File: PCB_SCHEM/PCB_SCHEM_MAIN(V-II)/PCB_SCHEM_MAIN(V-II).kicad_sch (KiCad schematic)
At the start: 26 parts, among them J1 USB_C_Receptacle_USB2.0_14P, SW1 SW_Push, U1 RP2040, U2 TPS61291DRVR, U3 LSM6DS3, U4 MX25L3233FM1, U5 MX25L3233FM1, Y1 Crystal_GND24

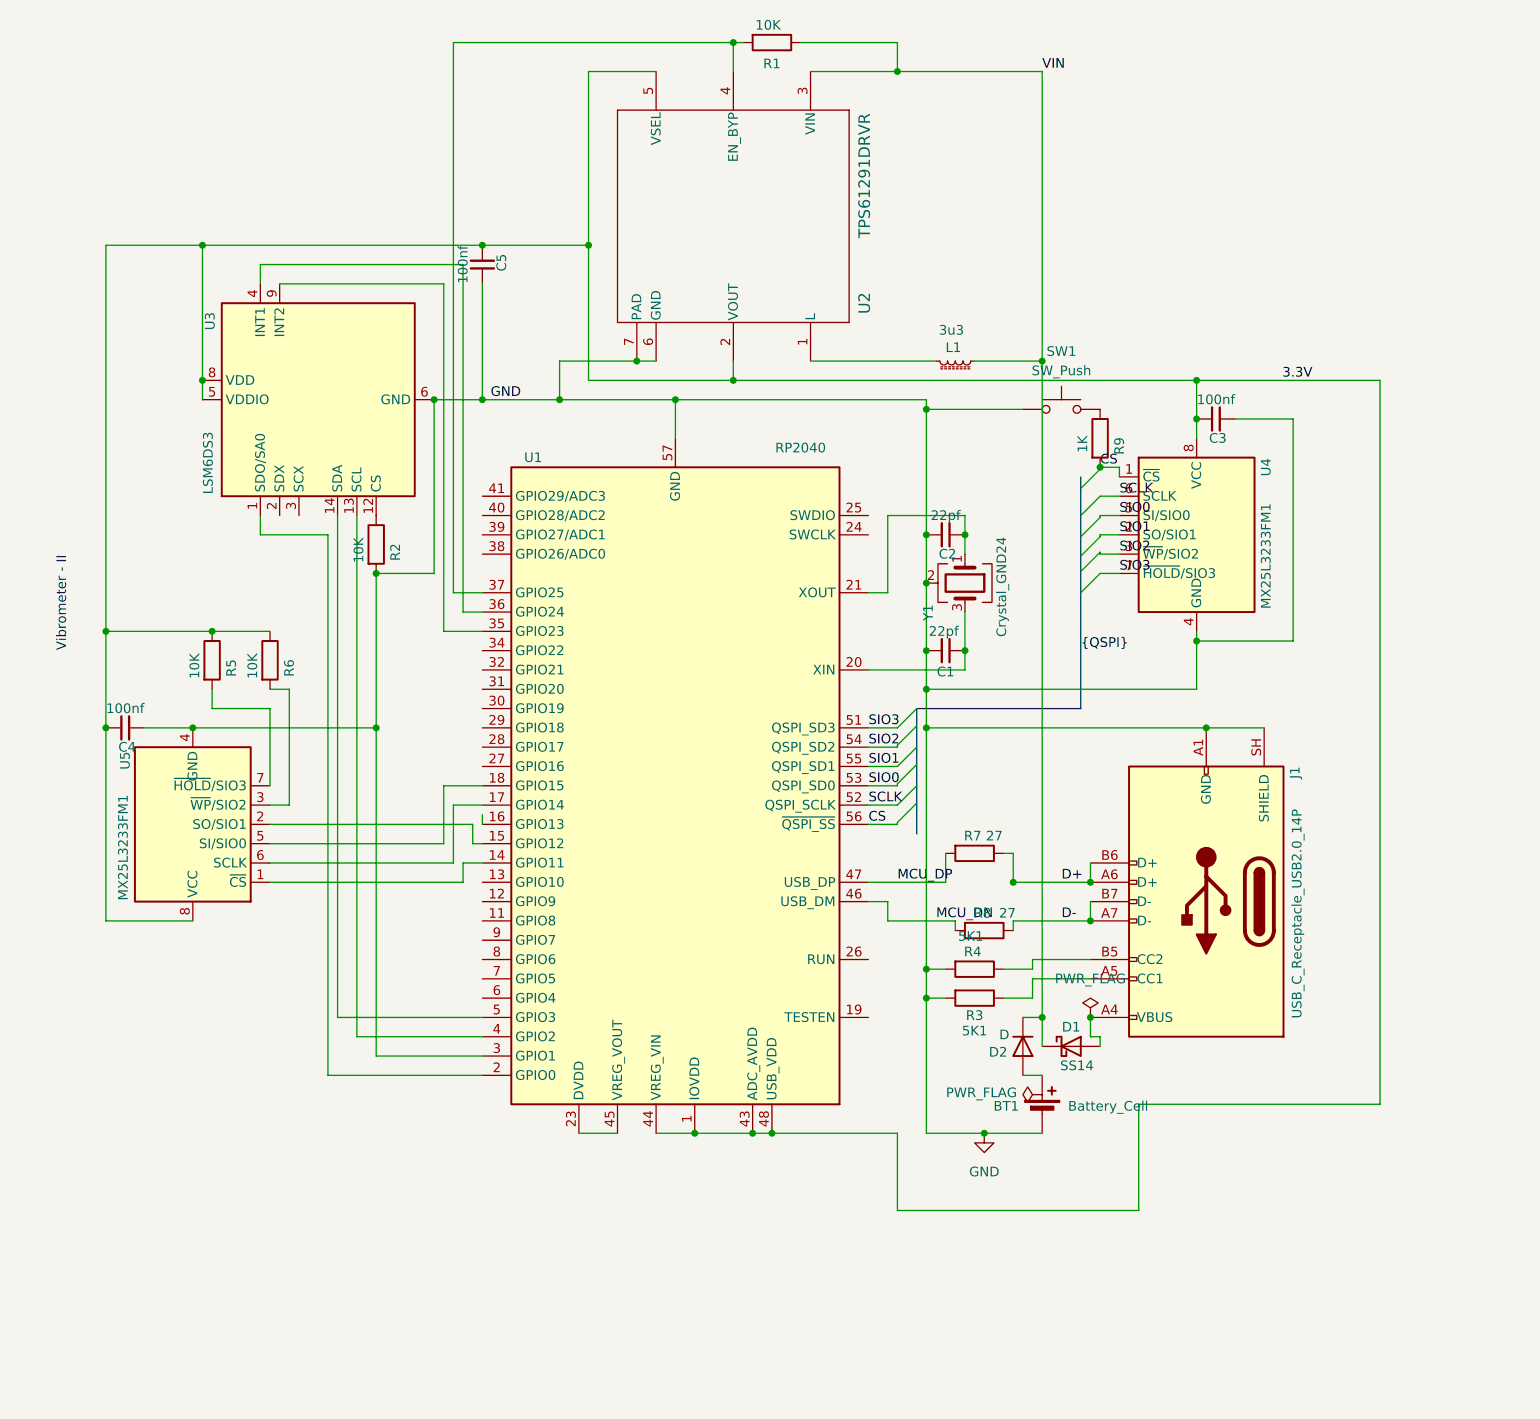
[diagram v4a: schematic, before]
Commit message: Added singature trademark to PCB design
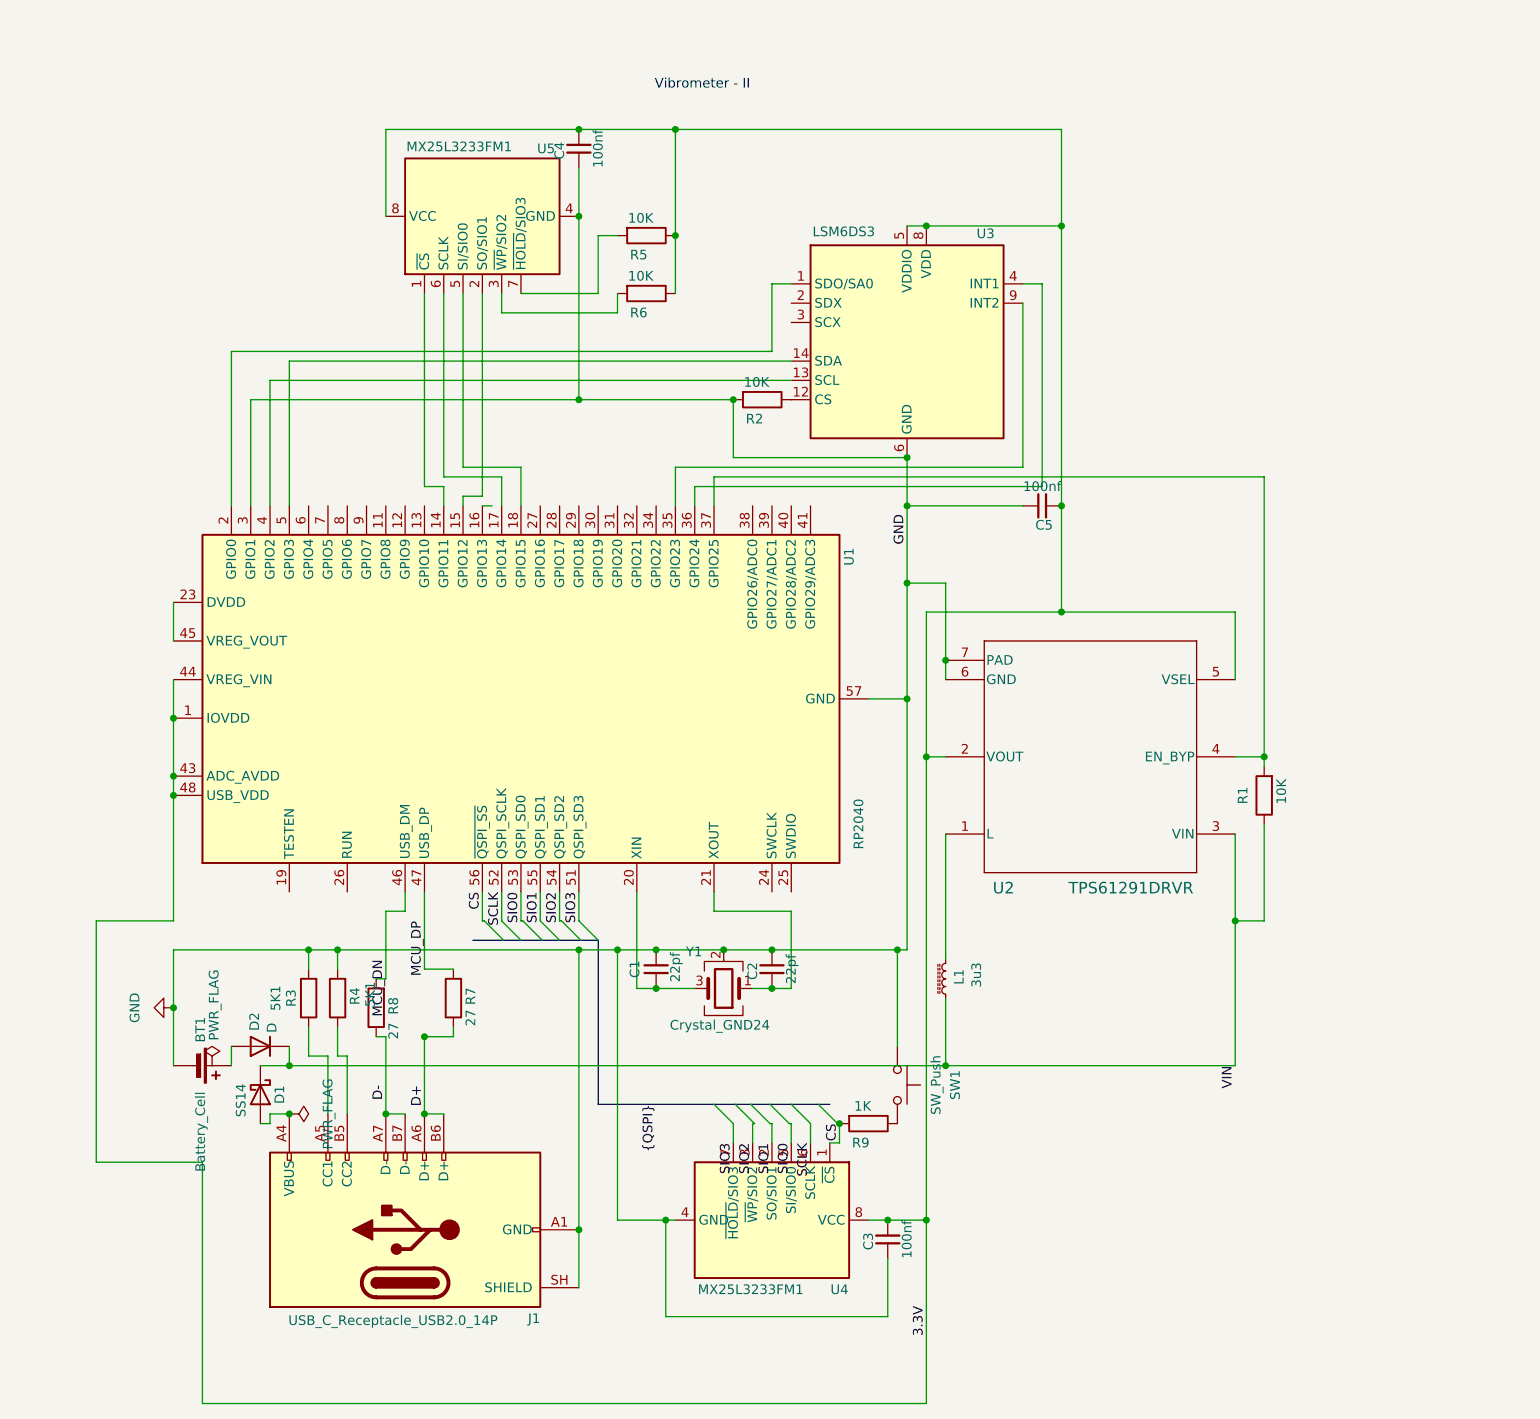
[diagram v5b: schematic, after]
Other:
- moved on the sheet: BT1, C1, C2, C3, C4, C5, D1, D2, J1, L1, R1, R2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

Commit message: Fixed major LSM6DS3 sleep function wiring error and furnished traces. Also added track to track teardrops. 3D view pictures also added.
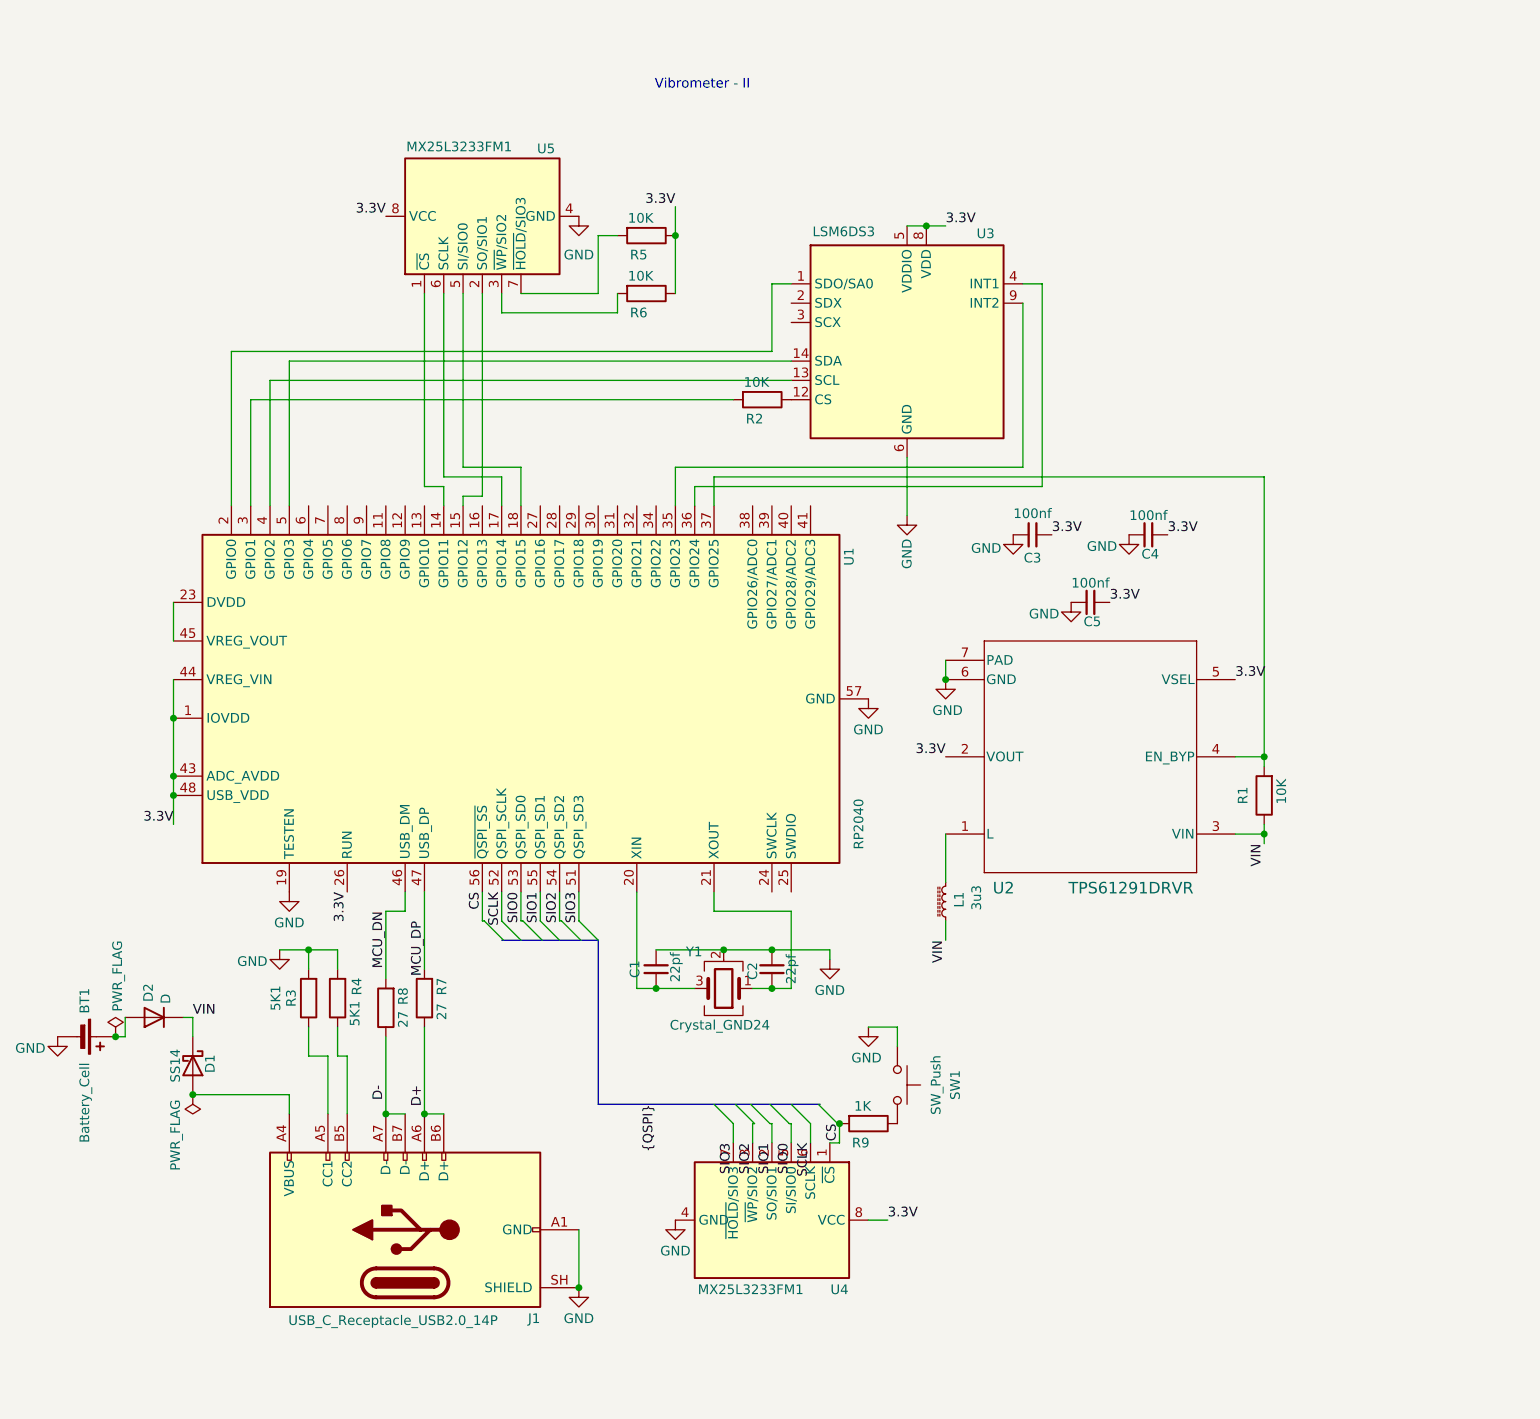
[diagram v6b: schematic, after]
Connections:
- net 3.3V: now also C4.1, U1.26 (RUN); no longer C4.2
- net GND: now also C4.2, U1.19 (TESTEN); no longer C4.1, R2.2, U1.3 (GPIO1)
- new net: R2.2, U1.3 (GPIO1)
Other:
- moved on the sheet: BT1, C3, C4, C5, D1, D2, L1, R7, R8
